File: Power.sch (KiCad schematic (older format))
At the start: 35 parts, among them J1 USB_MINIB, J2 TEST_1P, J3 TEST_1P, U1 FT230XS, U2 TPS562200, U3 AP2210-3.3, U4 AP2204K-5.0

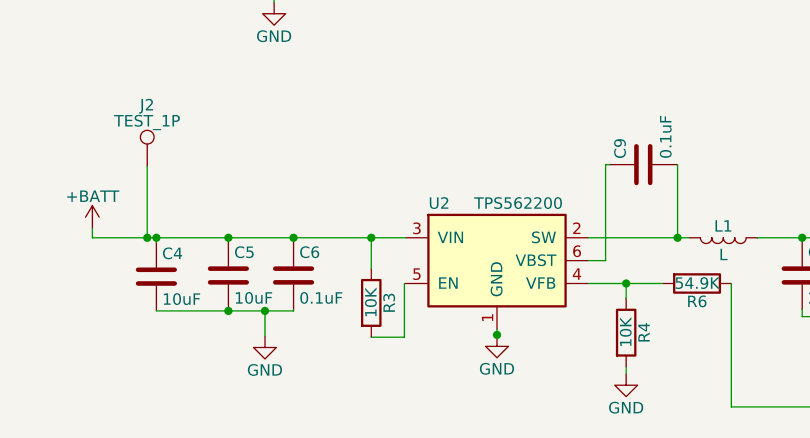
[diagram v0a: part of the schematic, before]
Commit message: Bring schematic in line with PCB. Previous update broke this.
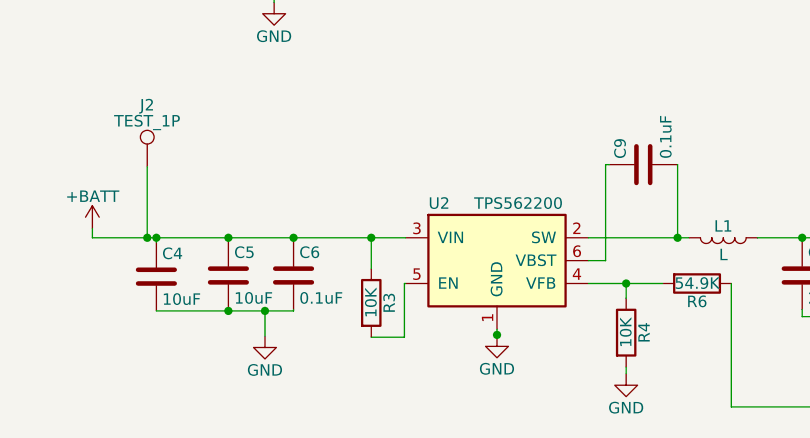
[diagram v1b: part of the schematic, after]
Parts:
- C1, C10, C11, C12, C13, C14, C15, C2, C3, C4, C5, C6, C7, C8, C9: footprint Capacitor_SMD:C_0603_1608Metric -> Capacitors_SMD:C_0603
- J2, J3: footprint TestPoint:TestPoint_Pad_D2.0mm -> Connectors_TestPoints:Test_Point_Pad_d1.5mm
- R1, R2, R3, R4, R5, R6, R7, R8: footprint Resistor_SMD:R_0603_1608Metric -> Resistors_SMD:R_0603
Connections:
- net at U2.5 (EN): now also R3.2

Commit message: Changes based on review reccommemdations
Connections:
- net +3V3: no longer R5.1, R7.2
- new net: R5.1, R7.2
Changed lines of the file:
@@
 Text Notes 3915 1570 0    39   ~ 0
 FTDI decoupling
-$Comp
-L +3.3V #PWR09
-U 1 1 5A1B6823
-P 5585 2155
-F 0 "#PWR09" H 5585 2005 50  0001 C CNN
-F 1 "+3.3V" H 5585 2295 50  0000 C CNN
-F 2 "" H 5585 2155 50  0001 C CNN
-F 3 "" H 5585 2155 50  0001 C CNN
-	1    5585 2155
-	1    0    0    -1
-$EndComp
 Text Notes 2385 850  0    79   ~ 0
 USB Power
@@
 3.3V Regulation
 $Comp
-L GND #PWR010
+L GND #PWR09
 U 1 1 5A1BD31A
 P 8495 3460
-F 0 "#PWR010" H 8495 3210 50  0001 C CNN
+F 0 "#PWR09" H 8495 3210 50  0001 C CNN
 F 1 "GND" H 8495 3310 50  0000 C CNN
 F 2 "" H 8495 3460 50  0001 C CNN
@@
 5V LDO Regulation
 $Comp
-L VBUS #PWR011
+L VBUS #PWR010
 U 1 1 5A221E30
 P 3685 1850
-F 0 "#PWR011" H 3685 1700 50  0001 C CNN
+F 0 "#PWR010" H 3685 1700 50  0001 C CNN
 F 1 "VBUS" H 3685 2000 50  0000 C CNN
 F 2 "" H 3685 1850 50  0001 C CNN
@@
 $EndComp
 $Comp
-L GND #PWR012
+L GND #PWR011
 U 1 1 59E266CE
 P 2035 3600
-F 0 "#PWR012" H 2035 3350 50  0001 C CNN
+F 0 "#PWR011" H 2035 3350 50  0001 C CNN
 F 1 "GND" H 2035 3450 50  0000 C CNN
 F 2 "" H 2035 3600 50  0001 C CNN
@@
 $EndComp
 $Comp
-L +BATT #PWR013
+L +BATT #PWR012
 U 1 1 5AD2DEE0
 P 7445 3460
-F 0 "#PWR013" H 7445 3310 50  0001 C CNN
+F 0 "#PWR012" H 7445 3310 50  0001 C CNN
 F 1 "+BATT" H 7445 3600 50  0000 C CNN
 F 2 "" H 7445 3460 50  0001 C CNN
@@
 $EndComp
 $Comp
-L VCC #PWR014
+L VCC #PWR013
 U 1 1 5AD2E526
 P 6965 3175
-F 0 "#PWR014" H 6965 3025 50  0001 C CNN
+F 0 "#PWR013" H 6965 3025 50  0001 C CNN
 F 1 "VCC" H 6965 3325 50  0000 C CNN
 F 2 "" H 6965 3175 50  0001 C CNN
@@
 $EndComp
 $Comp
-L GND #PWR015
+L GND #PWR014
 U 1 1 5AD2F48E
 P 8505 4695
-F 0 "#PWR015" H 8505 4445 50  0001 C CNN
+F 0 "#PWR014" H 8505 4445 50  0001 C CNN
 F 1 "GND" H 8505 4545 50  0000 C CNN
 F 2 "" H 8505 4695 50  0001 C CNN
@@
 Output Max 150mA
 $Comp
-L +5V #PWR016
+L +5V #PWR015
 U 1 1 5AD30E37
 P 8965 4160
-F 0 "#PWR016" H 8965 4010 50  0001 C CNN
+F 0 "#PWR015" H 8965 4010 50  0001 C CNN
 F 1 "+5V" H 8965 4300 50  0000 C CNN
 F 2 "" H 8965 4160 50  0001 C CNN
@@
 	8495 3240 8495 3460
 Wire Wire Line
-	3885 2275 3085 2275
+	3085 2275 5160 2275
 Wire Wire Line
 	3685 1850 3685 2375
-Wire Wire Line
-	5585 2155 5585 2180
 Connection ~ 5585 2180
 Wire Wire Line
@@
 Connection ~ 4110 4905
 $Comp
-L GND #PWR017
+L GND #PWR016
 U 1 1 5AE41892
 P 3645 5335
-F 0 "#PWR017" H 3645 5085 50  0001 C CNN
+F 0 "#PWR016" H 3645 5085 50  0001 C CNN
 F 1 "GND" H 3645 5185 50  0000 C CNN
 F 2 "" H 3645 5335 50  0001 C CNN
@@
 Connection ~ 3645 5225
 $Comp
-L GND #PWR018
+L GND #PWR017
 U 1 1 5AE41DA7
 P 5225 5500
-F 0 "#PWR018" H 5225 5250 50  0001 C CNN
+F 0 "#PWR017" H 5225 5250 50  0001 C CNN
 F 1 "GND" H 5225 5350 50  0000 C CNN
 F 2 "" H 5225 5500 50  0001 C CNN
@@
 Connection ~ 6255 4905
 $Comp
-L GND #PWR019
+L GND #PWR018
 U 1 1 5AE4232A
 P 6130 5250
-F 0 "#PWR019" H 6130 5000 50  0001 C CNN
+F 0 "#PWR018" H 6130 5000 50  0001 C CNN
 F 1 "GND" H 6130 5100 50  0000 C CNN
 F 2 "" H 6130 5250 50  0001 C CNN
@@
 $EndComp
 $Comp
-L +BATT #PWR020
+L +BATT #PWR019
 U 1 1 5AE44BDA
 P 2890 4865
-F 0 "#PWR020" H 2890 4715 50  0001 C CNN
+F 0 "#PWR019" H 2890 4715 50  0001 C CNN
 F 1 "+BATT" H 2890 5005 50  0000 C CNN
 F 2 "" H 2890 4865 50  0001 C CNN
@@
 Connection ~ 3170 4905
 $Comp
-L VCC #PWR021
+L VCC #PWR020
 U 1 1 5AE45325
 P 7895 2590
-F 0 "#PWR021" H 7895 2440 50  0001 C CNN
+F 0 "#PWR020" H 7895 2440 50  0001 C CNN
 F 1 "VCC" H 7895 2740 50  0000 C CNN
 F 2 "" H 7895 2590 50  0001 C CNN
@@
 Connection ~ 3130 4905
 $Comp
-L +5VP #PWR022
+L +5VP #PWR021
 U 1 1 5AE46242
 P 6700 4800
-F 0 "#PWR022" H 6700 4650 50  0001 C CNN
+F 0 "#PWR021" H 6700 4650 50  0001 C CNN
 F 1 "+5VP" H 6700 4940 50  0000 C CNN
 F 2 "" H 6700 4800 50  0001 C CNN
@@
 Connection ~ 6420 4905
 $Comp
-L GND #PWR023
+L GND #PWR022
 U 1 1 5AE4C2DE
 P 4660 5330
-F 0 "#PWR023" H 4660 5080 50  0001 C CNN
+F 0 "#PWR022" H 4660 5080 50  0001 C CNN
 F 1 "GND" H 4660 5180 50  0000 C CNN
 F 2 "" H 4660 5330 50  0001 C CNN
@@
 Connection ~ 4660 5330
 $Comp
-L +BATT #PWR024
+L +BATT #PWR023
 U 1 1 5AE4D18E
 P 7895 4130
-F 0 "#PWR024" H 7895 3980 50  0001 C CNN
+F 0 "#PWR023" H 7895 3980 50  0001 C CNN
 F 1 "+BATT" H 7895 4270 50  0000 C CNN
 F 2 "" H 7895 4130 50  0001 C CNN
@@
 Wire Wire Line
 	4255 5105 4255 5340
+Wire Wire Line
+	5160 2275 5160 2100
+Wire Wire Line
+	5160 2100 5585 2100
+Wire Wire Line
+	5585 2100 5585 2175
+Connection ~ 3885 2275
 $EndSCHEMATC

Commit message: Final design published. Gerbers and PDF schematic generated
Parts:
- added J28: Conn_01x02, SOAR_Kicad_Library:TerminalBlock_5mm_2POS_ED2600, symbol Conn_01x02
- added Q1: Q_NMOS_GSD, TO_SOT_Packages_SMD:SOT-23, symbol Q_NMOS_GSD
- J1: footprint SOAR_Library:USB-Mini-B -> SOAR_Kicad_Library:USB-Mini-B
- L1: value L -> 4.7uH; footprint SOAR_Library:L_1008 -> SOAR_Kicad_Library:L_1008
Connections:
- net +5VP: now also Q1.3 (D)
- net GND: now also J28.2 (Pin_2)
- new net: J28.1 (Pin_1), Q1.2 (S)
- new net Fan_ctrl: Q1.1 (G)
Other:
- note added: "Set as puldown"
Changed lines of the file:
@@
 F 0 "J1" H 1135 3425 50  0000 L CNN
 F 1 "USB_MINIB" H 1135 3325 50  0000 L CNN
-F 2 "SOAR_Library:USB-Mini-B" H 1485 2925 50  0001 C CNN
+F 2 "SOAR_Kicad_Library:USB-Mini-B" H 1485 2925 50  0001 C CNN
 F 3 "http://files.edac.net/690-005-299-043.pdf" H 1485 2925 50  0001 C CNN
 F 4 "690-005-299-043" H 1335 2975 60  0001 C CNN "Digikey"
@@
 P 5650 4905
 F 0 "L1" V 5600 4905 50  0000 C CNN
-F 1 "L" V 5725 4905 50  0000 C CNN
-F 2 "SOAR_Library:L_1008" H 5650 4905 50  0001 C CNN
+F 1 "4.7uH" V 5725 4905 50  0000 C CNN
+F 2 "SOAR_Kicad_Library:L_1008" H 5650 4905 50  0001 C CNN
 F 3 "" H 5650 4905 50  0001 C CNN
 	1    5650 4905
@@
 	5585 2100 5585 2175
 Connection ~ 3885 2275
+$Comp
+L +5VP #PWR024
+U 1 1 5AFA66B7
+P 1625 4400
+F 0 "#PWR024" H 1625 4250 50  0001 C CNN
+F 1 "+5VP" H 1625 4540 50  0000 C CNN
+F 2 "" H 1625 4400 50  0001 C CNN
+F 3 "" H 1625 4400 50  0001 C CNN
+	1    1625 4400
+	1    0    0    -1
+$EndComp
+Wire Wire Line
+	1625 4400 1625 4450
+$Comp
+L Conn_01x02 J28
+U 1 1 5AFA6995
+P 1915 4925
+F 0 "J28" H 1915 5025 50  0000 C CNN
+F 1 "Conn_01x02" H 1915 4725 50  0000 C CNN
+F 2 "SOAR_Kicad_Library:TerminalBlock_5mm_2POS_ED2600" H 1915 4925 50  0001 C CNN
+F 3 "" H 1915 4925 50  0001 C CNN
+	1    1915 4925
+	1    0    0    -1
+$EndComp
+Wire Wire Line
+	1715 4925 1625 4925
+Wire Wire Line
+	1625 4925 1625 4850
+$Comp
+L GND #PWR025
+U 1 1 5AFA6DE2
+P 1710 5125
+F 0 "#PWR025" H 1710 4875 50  0001 C CNN
+F 1 "GND" H 1710 4975 50  0000 C CNN
+F 2 "" H 1710 5125 50  0001 C CNN
+F 3 "" H 1710 5125 50  0001 C CNN
+	1    1710 5125
+	1    0    0    -1
+$EndComp
+Wire Wire Line
+	1715 5025 1710 5025
+Wire Wire Line
+	1710 5025 1710 5125
+Text GLabel 1055 4650 0    39   Input ~ 0
+Fan_ctrl
+Wire Wire Line
+	1055 4650 1325 4650
+$Comp
+L Q_NMOS_GSD Q1
+U 1 1 5AFA8AD0
+P 1525 4650
+F 0 "Q1" H 1725 4700 50  0000 L CNN
+F 1 "Q_NMOS_GSD" H 1725 4600 50  0000 L CNN
+F 2 "TO_SOT_Packages_SMD:SOT-23" H 1725 4750 50  0001 C CNN
+F 3 "" H 1525 4650 50  0001 C CNN
+	1    1525 4650
+	1    0    0    -1
+$EndComp
+Text Notes 725  4785 0    39   ~ 0
+Set as puldown
 $EndSCHEMATC
